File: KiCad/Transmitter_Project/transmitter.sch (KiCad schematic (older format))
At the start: 12 parts, among them J1 RB1-125BAG1A, Q1 2N3904, Q2 2N3906, U1 LM7171

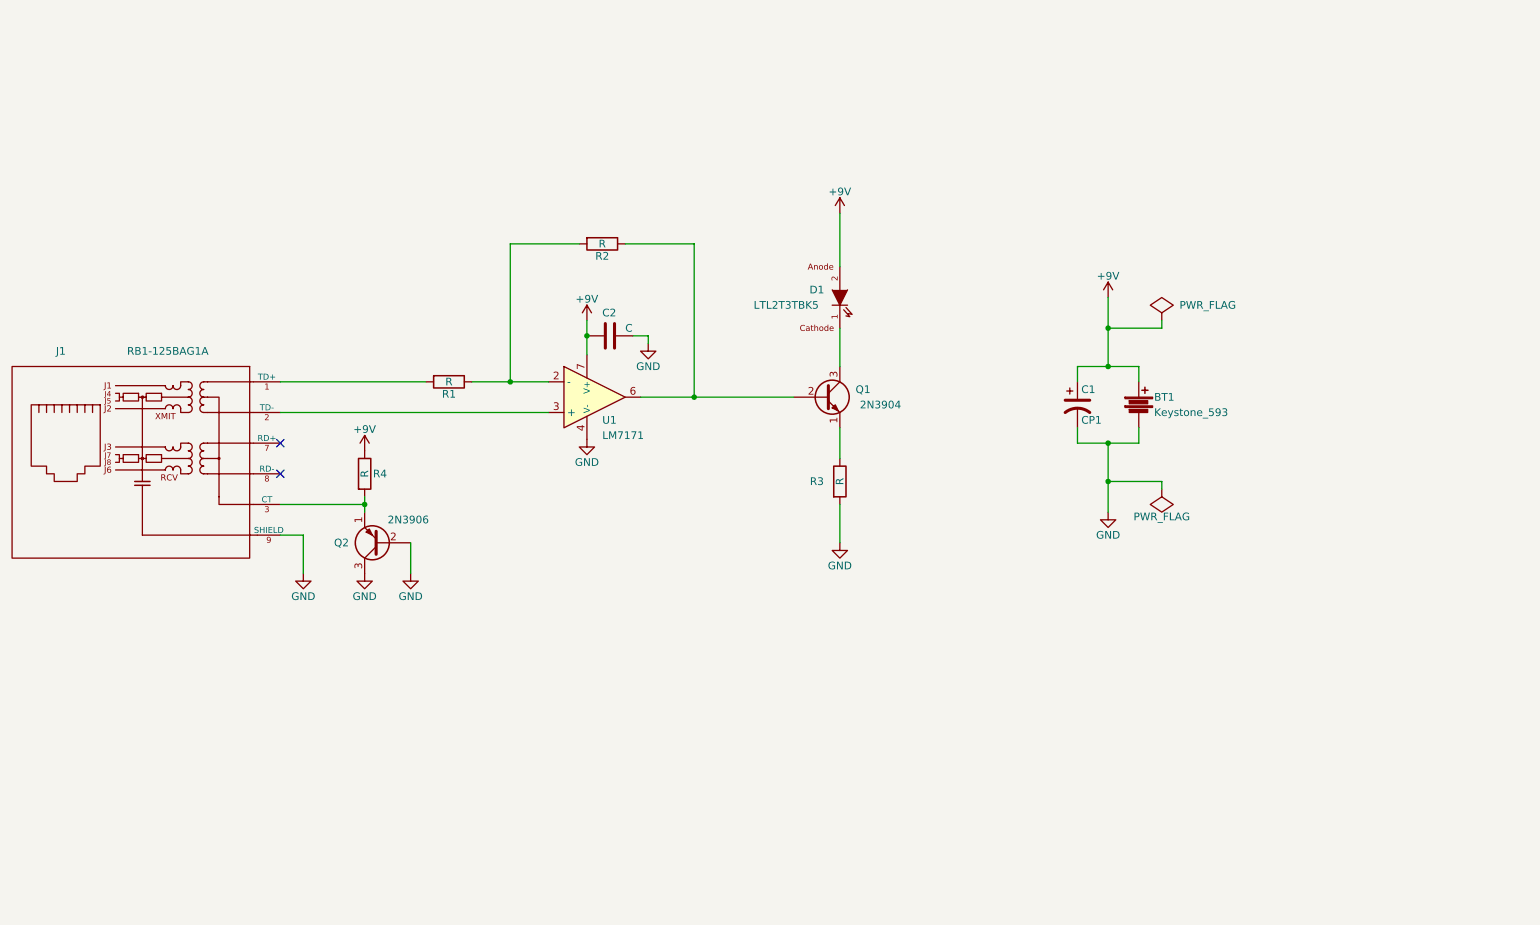
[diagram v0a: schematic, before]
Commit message: Transmitter complete and tested, receiver routed
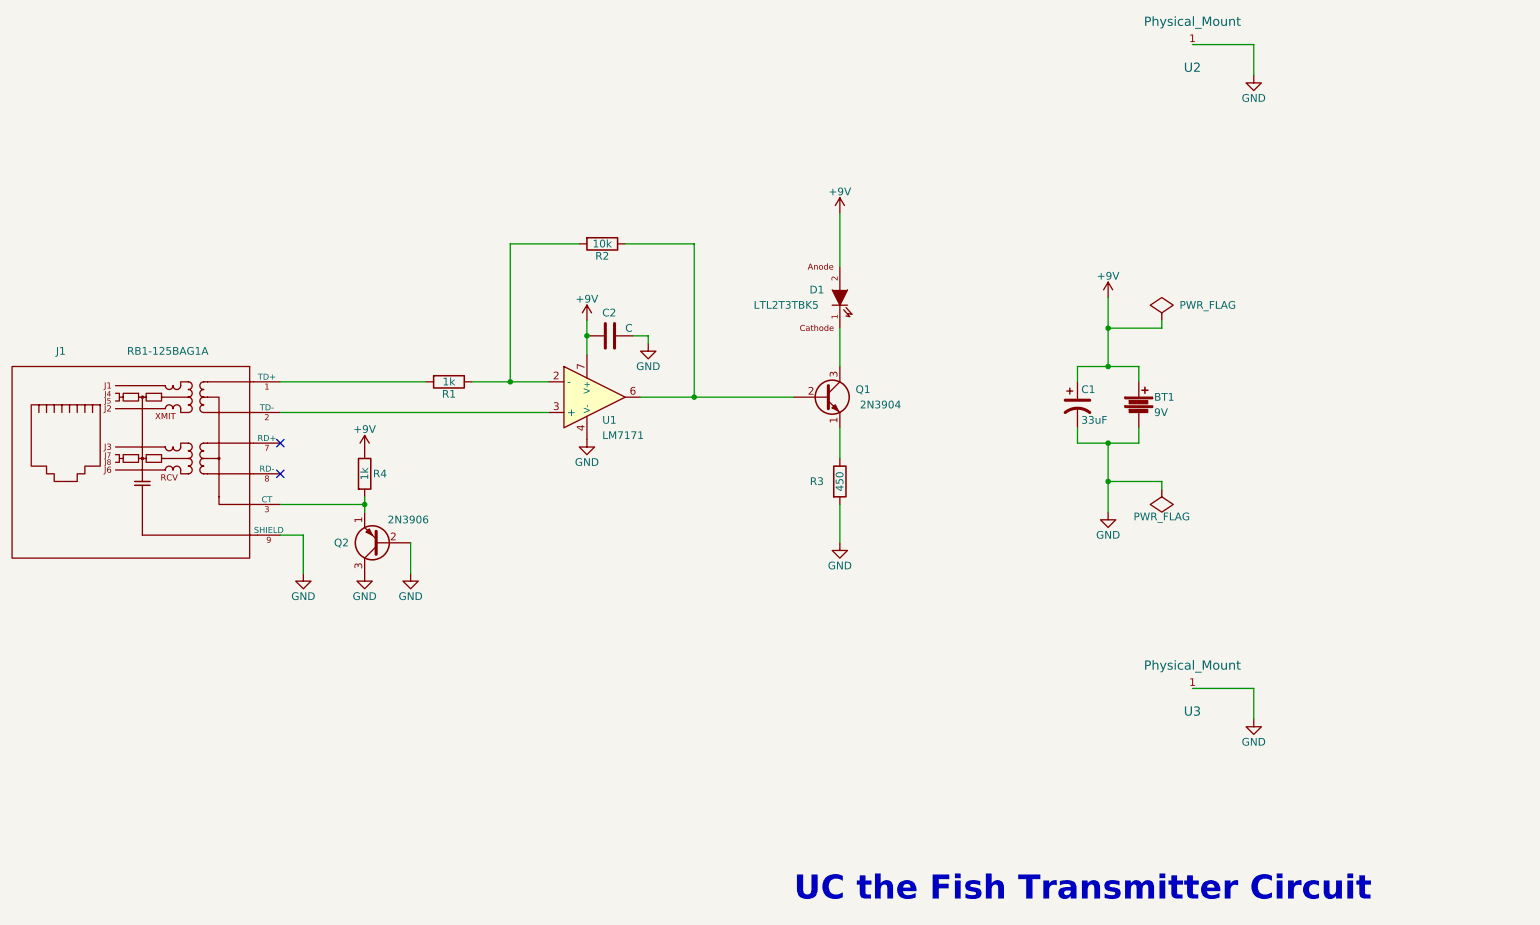
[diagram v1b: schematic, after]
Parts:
- added U2, U3: Physical_Mount, UC_the_Fish_Components:Mounting_Via, symbol Physical_Mount
- BT1: value Keystone_593 -> 9V
- C1: value CP1 -> 33uF; footprint (none) -> UC_the_Fish_Components:TAP107K006SCS
- C2: footprint (none) -> UC_the_Fish_Components:200Mil_Passive
- R1, R4: value R -> 1k; footprint (none) -> UC_the_Fish_Components:400Mil_Passive
- R2: value R -> 10k; footprint (none) -> UC_the_Fish_Components:400Mil_Passive
- R3: value R -> 450; footprint (none) -> UC_the_Fish_Components:400Mil_Passive
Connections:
- net GND: now also U2.1, U3.1
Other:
- note added: "UC the Fish Transmitter Circuit"
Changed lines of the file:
@@
 P 4950 3600
 F 0 "R1" V 5030 3600 50  0000 C CNN
-F 1 "R" V 4950 3600 50  0000 C CNN
-F 2 "" V 4880 3600 50  0000 C CNN
+F 1 "1k" V 4950 3600 50  0000 C CNN
+F 2 "UC_the_Fish_Components:400Mil_Passive" V 4880 3600 50  0001 C CNN
 F 3 "" H 4950 3600 50  0000 C CNN
 	1    4950 3600
@@
 P 5950 2700
 F 0 "R2" V 6030 2700 50  0000 C CNN
-F 1 "R" V 5950 2700 50  0000 C CNN
-F 2 "" V 5880 2700 50  0000 C CNN
+F 1 "10k" V 5950 2700 50  0000 C CNN
+F 2 "UC_the_Fish_Components:400Mil_Passive" V 5880 2700 50  0001 C CNN
 F 3 "" H 5950 2700 50  0000 C CNN
 	1    5950 2700
@@
 P 4400 4200
 F 0 "R4" H 4500 4200 50  0000 C CNN
-F 1 "R" V 4400 4200 50  0000 C CNN
-F 2 "" V 4330 4200 50  0000 C CNN
+F 1 "1k" V 4400 4200 50  0000 C CNN
+F 2 "UC_the_Fish_Components:400Mil_Passive" V 4330 4200 50  0001 C CNN
 F 3 "" H 4400 4200 50  0000 C CNN
 	1    4400 4200
@@
 P 7500 4250
 F 0 "R3" H 7350 4250 50  0000 C CNN
-F 1 "R" V 7500 4250 50  0000 C CNN
-F 2 "" V 7430 4250 50  0000 C CNN
+F 1 "450" V 7500 4250 50  0000 C CNN
+F 2 "UC_the_Fish_Components:400Mil_Passive" V 7430 4250 50  0001 C CNN
 F 3 "" H 7500 4250 50  0000 C CNN
 	1    7500 4250
@@
 P 9450 3750
 F 0 "BT1" H 9550 3800 50  0000 L CNN
-F 1 "Keystone_593" H 9550 3700 50  0000 L CNN
+F 1 "9V" H 9550 3700 50  0000 L CNN
 F 2 "UC_the_Fish_Components:9V_Contacts" H 8600 3750 50  0001 C CNN
 F 3 "" V 9450 3790 50  0000 C CNN
@@
 P 9050 3750
 F 0 "C1" H 9075 3850 50  0000 L CNN
-F 1 "CP1" H 9075 3650 50  0000 L CNN
-F 2 "" H 9050 3750 50  0000 C CNN
+F 1 "33uF" H 9075 3650 50  0000 L CNN
+F 2 "UC_the_Fish_Components:TAP107K006SCS" H 9050 3750 50  0001 C CNN
 F 3 "" H 9050 3750 50  0000 C CNN
 	1    9050 3750
@@
 F 0 "C2" V 5850 3250 50  0000 L CNN
 F 1 "C" V 5950 3400 50  0000 L CNN
-F 2 "" H 6038 3150 50  0000 C CNN
+F 2 "UC_the_Fish_Components:200Mil_Passive" H 6038 3150 50  0001 C CNN
 F 3 "" H 6000 3300 50  0000 C CNN
 	1    6000 3300
@@
 	9600 3250 9250 3250
 Connection ~ 9250 3250
+$Comp
+L GND #PWR014
+U 1 1 56F9475A
+P 10200 1600
+F 0 "#PWR014" H 10200 1350 50  0001 C CNN
+F 1 "GND" H 10200 1450 50  0000 C CNN
+F 2 "" H 10200 1600 50  0000 C CNN
+F 3 "" H 10200 1600 50  0000 C CNN
+	1    10200 1600
+	1    0    0    -1
+$EndComp
+$Comp
+L GND #PWR015
+U 1 1 56F94B58
+P 10200 5800
+F 0 "#PWR015" H 10200 5550 50  0001 C CNN
+F 1 "GND" H 10200 5650 50  0000 C CNN
+F 2 "" H 10200 5800 50  0000 C CNN
+F 3 "" H 10200 5800 50  0000 C CNN
+	1    10200 5800
+	1    0    0    -1
+$EndComp
+Wire Wire Line
+	9800 5600 10200 5600
+Wire Wire Line
+	10200 5600 10200 5800
+Wire Wire Line
+	9800 1400 10200 1400
+Wire Wire Line
+	10200 1400 10200 1600
+$Comp
+L Physical_Mount U2
+U 1 1 56F95418
+P 9800 1400
+F 0 "U2" H 9800 1250 60  0000 C CNN
+F 1 "Physical_Mount" H 9800 1550 60  0000 C CNN
+F 2 "UC_the_Fish_Components:Mounting_Via" H 9700 1150 60  0001 C CNN
+F 3 "" H 9800 1400 60  0000 C CNN
+	1    9800 1400
+	1    0    0    -1
+$EndComp
+$Comp
+L Physical_Mount U3
+U 1 1 56F95537
+P 9800 5600
+F 0 "U3" H 9800 5450 60  0000 C CNN
+F 1 "Physical_Mount" H 9800 5750 60  0000 C CNN
+F 2 "UC_the_Fish_Components:Mounting_Via" H 9700 5350 60  0001 C CNN
+F 3 "" H 9800 5600 60  0000 C CNN
+	1    9800 5600
+	1    0    0    -1
+$EndComp
+Text Notes 7200 7000 0    157  ~ 31
+UC the Fish Transmitter Circuit
 $EndSCHEMATC
